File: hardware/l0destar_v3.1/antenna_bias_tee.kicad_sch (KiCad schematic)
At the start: 12 parts

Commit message: update v3.1
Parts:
- removed S15D1: PESD5V0X1BL,315, libs:PESD5V0S1BL315, symbol PESD5V0X1BL_315:PESD5V0X1BL,315
- added S15D1, S15D2: TPD1E05U06DPYR, libs:DIO_TPD1E05U06DPYR, symbol TPD1E05U06DPYR:TPD1E05U06DPYR
- S15L1: value 47-100 nH, SRF > 2 GHz -> LQW18AN68NJ00D
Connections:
- net GND: now also S15D1.2 (GND), S15D2.2 (GND)
- net RF: now also S15D2.1 (I/O)
- net at S15J3.1 (In), S15J4.1: now also S15D1.1 (I/O)
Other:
- moved on the sheet: S15C1, S15C2, S15C3, S15C4, S15FB1, S15J1, S15J2, S15J4, S15L1, S15R1

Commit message: update v3.1
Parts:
- S15C1: Manufacturer_Name (none) -> Multicomp Pro; Manufacturer_Part_Number (none) -> 0402N470F500CT
- S15C2: Manufacturer_Name (none) -> Yageo; Manufacturer_Part_Number (none) -> AC0402FRNPO9BN101
- S15C3: Manufacturer_Name (none) -> Murata; Manufacturer_Part_Number (none) -> GRM1555CYA103JE01D
- S15C4: Manufacturer_Name (none) -> Kyocera AVX; Manufacturer_Part_Number (none) -> KAM05CR71A105KH
- S15D1, S15D2: Availability In Stock -> (none); Check_prices https://www.snapeda.com/parts/TPD1E05U06DPYR/Texas+Instrume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 -> (none); MF Texas Instruments -> (none); MP TPD1E05U06DPYR -> (none); Manufacturer_Name (none) -> Texas Instruments; Manufacturer_Part_Number (none) -> TPD1E05U06DPYR; Package X1SON-2 Texas Instruments -> (none); Price None -> (none); SnapEDA_Link https://www.snapeda.com/parts/TPD1E05U06DPYR/Texas+Instrume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 -> (none)
- S15FB1: Manufacturer_Name (none) -> Murata; Manufacturer_Part_Number (none) -> BLM15PX601SZ1D
- S15J1, S15J3: Manufacturer_Name (none) -> Hirose; Manufacturer_Part_Number (none) -> U.FL-R-SMT(01)
- S15J2, S15J4: Availability In Stock -> (none); Check_prices https://www.snapeda.com/parts/SMA-J-P-H-RA-TH1/Samtec+Inc./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 -> (none); MF Samtec -> (none); MP SMA-J-P-H-RA-TH1 -> (none); Manufacturer_Name (none) -> Samtec; Manufacturer_Part_Number (none) -> SMA-J-P-H-RA-TH1; Package None -> (none); Price None -> (none); Purchase-URL https://www.snapeda.com/api/url_track_click_mouser/?unipart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 -> (none); SnapEDA_Link https://www.snapeda.com/parts/SMA-J-P-H-RA-TH1/Samtec+Inc./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 -> (none)
- S15L1: Manufacturer_Name (none) -> Murata; Manufacturer_Part_Number (none) -> LQW18AN68NJ00D
- S15R1: Manufacturer_Name (none) -> CGS / TE Connectivity; Manufacturer_Part_Number (none) -> 3430A2F15RTDF

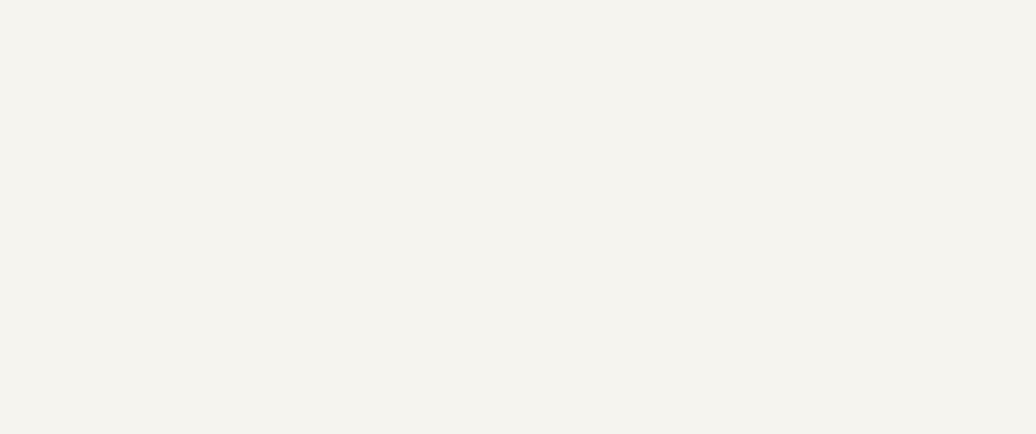
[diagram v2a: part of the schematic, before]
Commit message: update sheet annotations
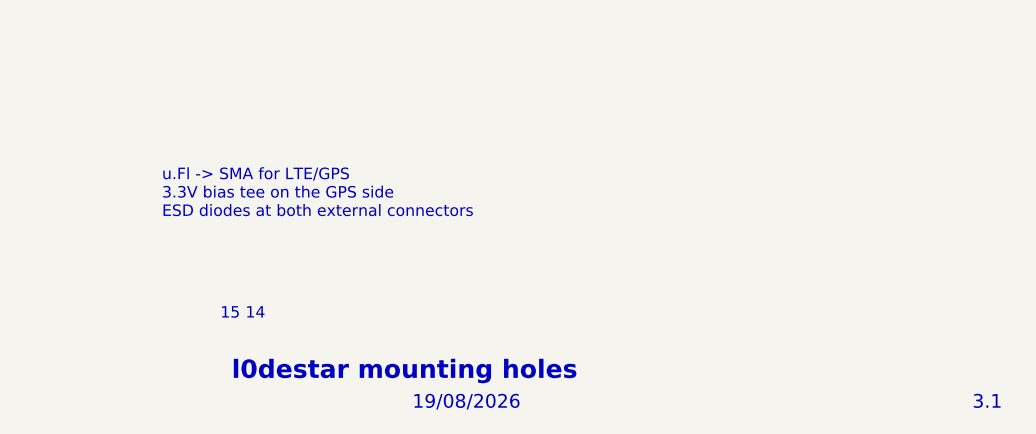
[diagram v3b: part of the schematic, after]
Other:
- note added: "14"
- note added: "15"
- note added: "19/08/2026"
- note added: "3.1"
- note added: "l0destar mounting holes"
- note added: "u.Fl -> SMA for LTE/GPS 3.3V bias tee on the GPS side ESD diodes at both external connectors"
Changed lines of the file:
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@@
 	(generator_version "10.0")
 	(paper "A4")
+	(text "l0destar mounting holes"
+		(exclude_from_sim no)
+		(at 186.182 189.865 0)
+		(effects
+			(font
+				(face "KiCad Font")
+				(size 2.032 2.032)
+				(thickness 0.4064)
+				(bold yes)
+			)
+			(justify left)
+		)
+	)
+	(text "14"
+		(exclude_from_sim no)
+		(at 187.706 183.515 0)
+		(effects
+			(font
+				(size 1.27 1.27)
+			)
+			(justify left)
+		)
+	)
+	(text "15"
+		(exclude_from_sim no)
+		(at 184.912 183.515 0)
+		(effects
+			(font
+				(size 1.27 1.27)
+			)
+			(justify left)
+		)
+	)
+	(text "19/08/2026"
+		(exclude_from_sim no)
+		(at 206.248 193.421 0)
+		(effects
+			(font
+				(face "KiCad Font")
+				(size 1.524 1.524)
+				(thickness 0.1905)
+			)
+			(justify left)
+		)
+	)
+	(text "3.1"
+		(exclude_from_sim no)
+		(at 268.478 193.421 0)
+		(effects
+			(font
+				(face "KiCad Font")
+				(size 1.524 1.524)
+				(thickness 0.1905)
+			)
+			(justify left)
+		)
+	)
+	(text "u.Fl -> SMA for LTE/GPS\n3.3V bias tee on the GPS side\nESD diodes at both external connectors"
+		(exclude_from_sim no)
+		(at 178.435 170.18 0)
+		(effects
+			(font
+				(size 1.27 1.27)
+			)
+			(justify left)
+		)
+	)
 	(junction
 		(at 72.39 98.425)

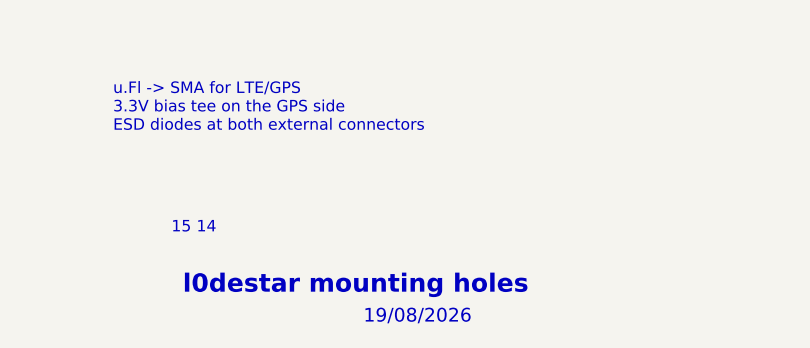
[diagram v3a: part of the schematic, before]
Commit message: fix sheet annotations
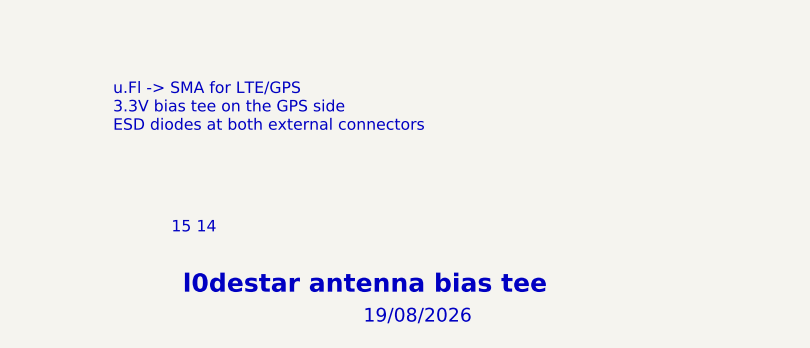
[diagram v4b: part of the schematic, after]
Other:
- note added: "l0destar antenna bias tee"
- note removed: "l0destar mounting holes"
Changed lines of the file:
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@@
 	(generator_version "10.0")
 	(paper "A4")
-	(text "l0destar mounting holes"
+	(text "l0destar antenna bias tee"
 		(exclude_from_sim no)
 		(at 186.182 189.865 0)

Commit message: schematic<>readme discrepency fixes
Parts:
- S15C1: value 0402 47pF 10V 5% C0G/NP0 -> 0402 47pF 50V 5% C0G/NP0
- S15C2: value 0402 100pF 10V 5% C0G/NP0 -> 0402 100pF 50V 5% C0G/NP0
- S15C3: value 0402 10nF 10V 5% C0G/NP0 -> 0402 10nF 50V 5% C0G/NP0
- S15R1: value 0508 1W 1% 15R -> 0508 1W 5% 15R
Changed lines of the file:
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@@
 			)
 		)
-		(property "Value" "0402 10nF 10V 5% C0G/NP0"
+		(property "Value" "0402 10nF 50V 5% C0G/NP0"
 			(at 145.415 76.8349 0)
 			(show_name no)
@@
 			)
 		)
-		(property "Value" "0402 100pF 10V 5% C0G/NP0"
+		(property "Value" "0402 100pF 50V 5% C0G/NP0"
 			(at 106.68 76.8349 0)
 			(show_name no)
@@
 			)
 		)
-		(property "Value" "0402 47pF 10V 5% C0G/NP0"
+		(property "Value" "0402 47pF 50V 5% C0G/NP0"
 			(at 49.53 81.915 90)
 			(show_name no)
@@
 			)
 		)
-		(property "Value" "0508 1W 1% 15R"
+		(property "Value" "0508 1W 5% 15R"
 			(at 41.91 62.865 90)
 			(show_name no)
